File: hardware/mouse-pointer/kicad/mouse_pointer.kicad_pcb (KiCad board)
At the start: 2 copper layers, 23.5 x 31.5 mm, 24 parts, among them J1 Conn_PinHeader, J2 Conn_FPC, U1 PMW3610, U2 TLV74318PDBVR

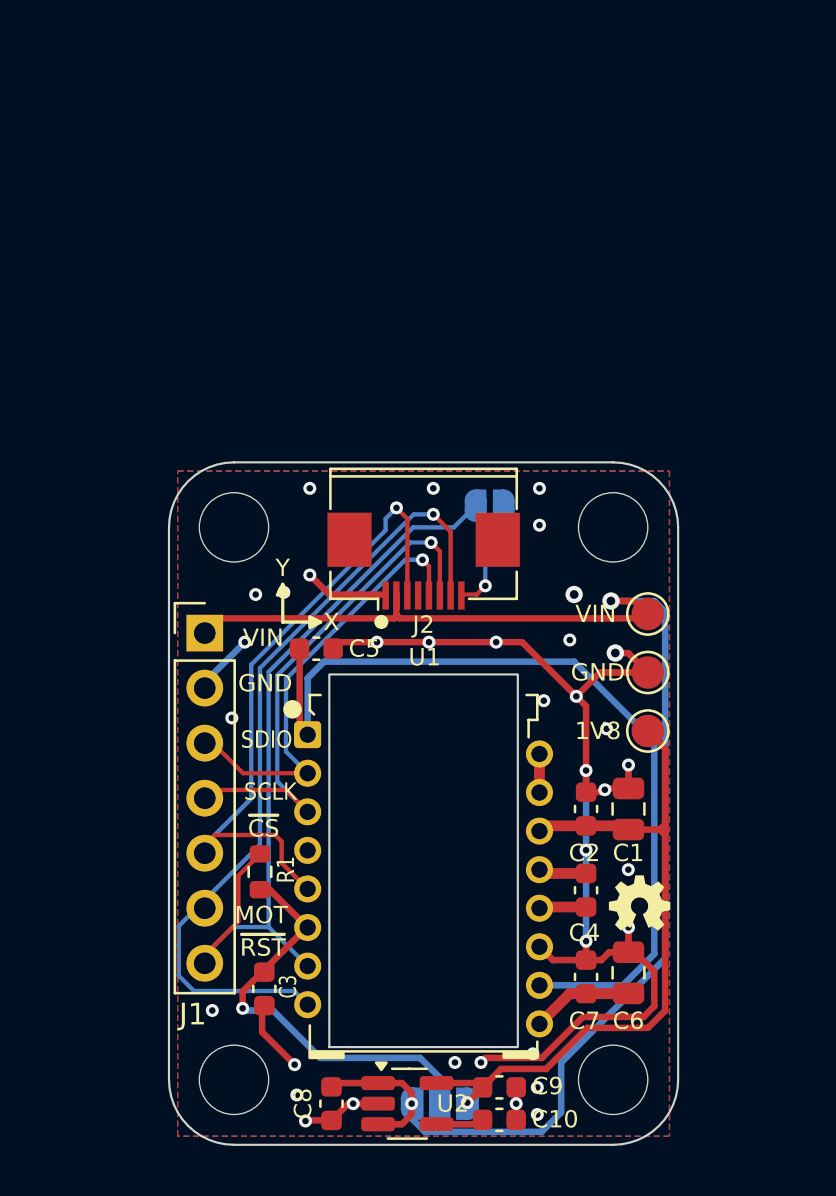
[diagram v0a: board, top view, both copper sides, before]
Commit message: feat: add RJ45 mouse pointer board interface
- Add the ClickTapToe 8P8C/RJ45 pinout to the PMW3610 mouse pointer board.
  - Add reset and VDDIO configuration links, optional nCS pull-up, and MOTION series resistor.
  - Extend the board layout for the RJ45 connector and added mounting holes.
  - Document revised mouse pointer cabling, twisted-pair grouping, and input hub wiring contract.
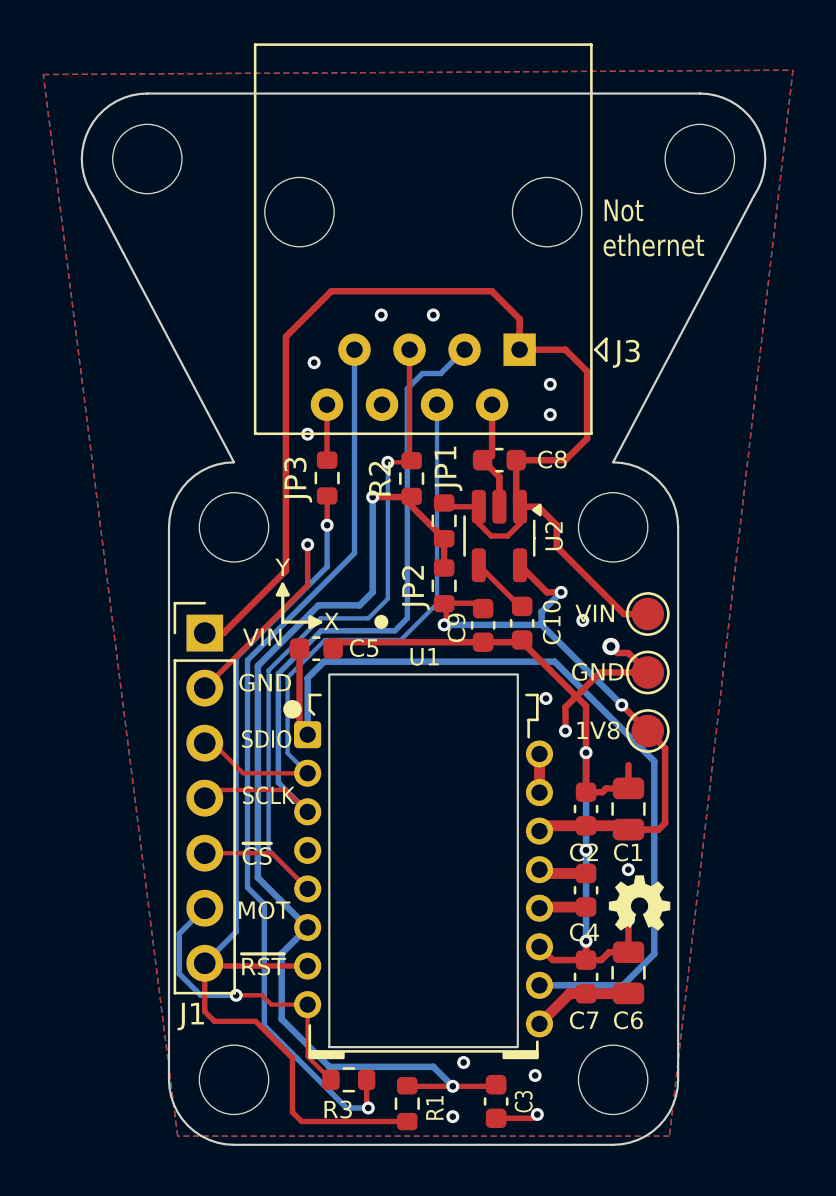
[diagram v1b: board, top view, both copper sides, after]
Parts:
- removed J2: Conn_FPC, mouse_pointer:FPC_8P_0.5mm_AFC01-S08FCA-00
- added H5: MountingHole, MountingHole:MountingHole_3.2mm_M3_ISO14580, B.Cu at (162.8, 70.2)
- added H6: MountingHole, MountingHole:MountingHole_3.2mm_M3_ISO14580, B.Cu at (137.2, 70.2)
- added J3: 8P8C, Connector_RJ:RJ45_Amphenol_54602-x08_Horizontal, F.Cu at (154.4, 79.0)
- added JP3: 0R, Resistor_SMD:R_0603_1608Metric, F.Cu at (145.6, 85.0)
- added R2: 100k, Resistor_SMD:R_0603_1608Metric, F.Cu at (149.4, 85.0)
- added R3: 100, Resistor_SMD:R_0603_1608Metric, F.Cu at (146.6, 112.8)
- JP1: value SolderJumper_3_Open -> 0R; footprint Jumper:SolderJumper-3_P1.3mm_Open_RoundedPad1.0x1.5mm_NumberLabels -> Resistor_SMD:R_0603_1608Metric; moved to F.Cu
- JP2: value FPC_RST -> 0R; footprint Jumper:SolderJumper-2_P1.3mm_Open_RoundedPad1.0x1.5mm -> Resistor_SMD:R_0603_1608Metric; moved to F.Cu
- moved C8 30.7 mm to (153.5, 84.2), turned to 180 degrees
- moved JP1 26.9 mm to (150.9, 87.0), turned to -90 degrees
- moved U2 26.5 mm to (153.5, 87.7), turned to -90 degrees
- moved C10 22.9 mm to (154.6, 91.7), turned to -90 degrees
- moved C9 21.3 mm to (152.8, 91.8), turned to -90 degrees
- moved R1 12.7 mm to (149.2, 113.8), turned to -90 degrees
- moved C3 11.9 mm to (153.3, 113.8)
- moved JP2 4.25 mm to (150.9, 90.0), turned to -90 degrees
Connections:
- JP2 pad 1: nRESET -> VDDIO
- JP2 pad 2: Net-(J2-Pin_8) -> +1V8
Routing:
- net MOT_RJ45: track 0.00 -> 41.3 mm, vias 0 -> 1
- net VDDIO: track 19.9 -> 48.3 mm, vias 1 -> 2
- net MOTION: track 37.4 -> 14.1 mm
- net VIN: track 66.4 -> 56.7 mm, vias 2 -> 0
- net SCLK: track 24.3 -> 33.1 mm, vias 1 -> 0
- net nRESET: track 36.3 -> 43.9 mm, vias 0 -> 1
- net SDIO: track 20.5 -> 27.8 mm, vias 1 -> 0
- net GND: track 66.4 -> 59.3 mm, vias 36 -> 20
- net nCS: track 30.0 -> 35.6 mm
- net Net-(J2-Pin_8): track 5.32 -> 0.00 mm, vias 1 -> 0
- net +1V8: track 33.4 -> 29.5 mm, vias 1 -> 3
- net nRST_RJ45: track 0.00 -> 2.56 mm
- net Net-(U2-NC): track 2.21 -> 2.79 mm
- net Net-(U1-+VCSEL): track 40.5 -> 40.0 mm
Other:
- board size 23.5 x 31.5 mm -> 31.5 x 48.5 mm
- board text added: "JP1: V_{DDIO}=VIN JP2: V_{DDIO}=1.8V JP1 + JP2: V_{DDIO}=VIN=VDD"
- board text added: "Not ethernet"
- board text removed: "JP1: [1-2 3]V_{DDIO}=VIN [1 2-3]V_{DDIO}=1.8V"

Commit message: fix: refine mouse pointer board layout
- Adjust board outline edges.
- Reposition components for improved decoupling
- Tune trace routing and via placement
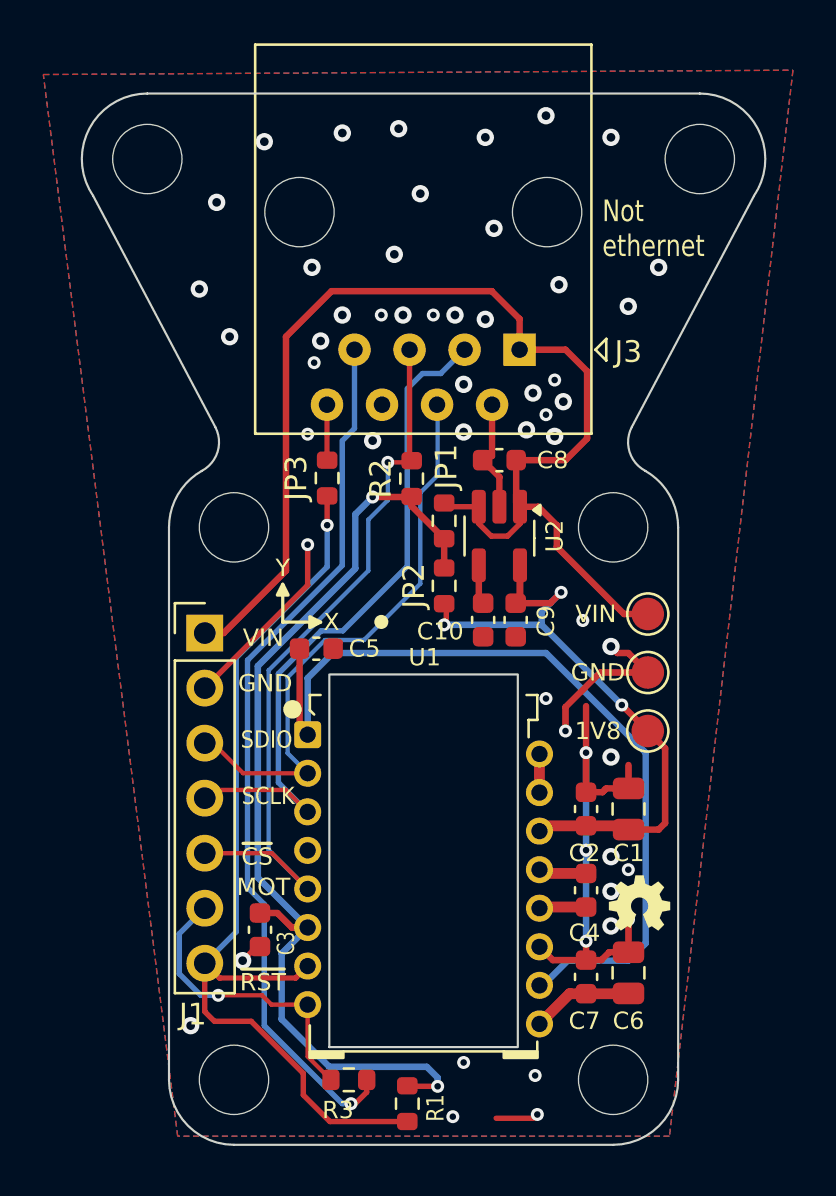
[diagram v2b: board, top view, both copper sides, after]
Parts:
- moved C3 13.5 mm to (142.4, 105.8)
- moved C10 1.81 mm to (152.8, 91.5)
- moved C9 1.52 mm to (154.2, 91.5)
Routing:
- net GND: track 59.3 -> 48.0 mm, vias 20 -> 54
- net VDDIO: track 48.3 -> 45.9 mm
- net SCLK: track 33.1 -> 31.7 mm
- net nCS: track 35.6 -> 34.4 mm
- net Net-(U2-NC): track 2.79 -> 1.55 mm
- net +1V8: track 29.5 -> 30.7 mm
- net SDIO: track 27.8 -> 26.8 mm
- net MOT_RJ45: track 41.3 -> 40.6 mm
- net Net-(U1-+VCSEL): track 40.0 -> 39.5 mm
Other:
- outline, holes or cut-outs redrawn

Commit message: feat: add ESD protection to mouse pointer and update board fields
- Add ESD protection, logo artwork, and final board manufacturing fields.
  - Include generated fabrication outputs for direct ordering.
  - Document hand-installed RJ45, optional tester header, and board configuration.
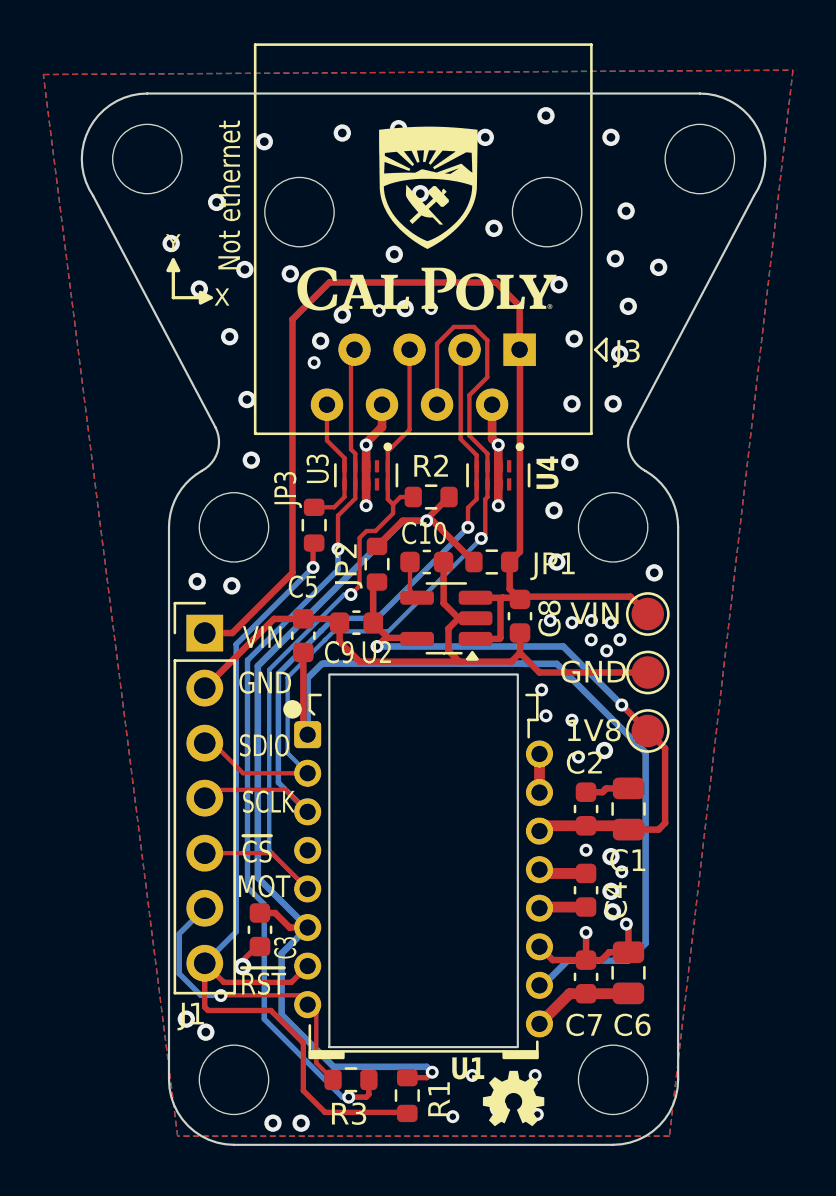
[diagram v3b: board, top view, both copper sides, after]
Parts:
- added U3: TPD4E05U06DQAR, mouse_pointer:IC_TPD4E05U06DQAR, F.Cu at (147.3, 84.8)
- added U4: TPD4E05U06DQAR, mouse_pointer:IC_TPD4E05U06DQAR, F.Cu at (153.4, 84.8)
- H3, H5, H6: moved to F.Cu
- moved C9 7.35 mm to (146.9, 91.7), turned to 180 degrees
- moved C8 7.26 mm to (154.4, 91.3), turned to -90 degrees
- moved U2 4.52 mm to (151.1, 91.5), turned to 180 degrees
- moved C10 3.73 mm to (150.2, 88.8), turned to 0 degrees
- moved JP2 3.26 mm to (147.8, 89.0)
- moved JP1 2.91 mm to (153.2, 88.8), turned to 180 degrees
- moved JP3 2.26 mm to (144.9, 87.2)
- moved R2 1.24 mm to (150.3, 85.8), turned to 180 degrees
- moved C5 0.85 mm to (144.4, 92.2), turned to 90 degrees
- moved R1 0.38 mm to (149.2, 113.5)
- moved R3 0.10 mm to (146.7, 112.8)
- turned H3 to 0 degrees
- turned H5 to 0 degrees
- turned H6 to 0 degrees
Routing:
- net SDIO: track 26.8 -> 37.6 mm, vias 0 -> 1
- net nRST_RJ45: track 2.56 -> 6.19 mm
- net GND: track 48.0 -> 51.2 mm, vias 54 -> 71
- net nRESET: track 43.4 -> 41.3 mm
- net VIN: track 56.7 -> 54.6 mm
- net nCS: track 34.4 -> 35.5 mm
- net VDDIO: track 45.9 -> 47.0 mm
- net +1V8: track 30.7 -> 29.8 mm, vias 3 -> 2
- net SCLK: track 31.7 -> 32.4 mm, vias 0 -> 1
- net MOT_RJ45: track 40.6 -> 40.5 mm, vias 1 -> 2

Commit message: feat: updated board for JLC constraints, add 3D models, add silkscreen logos, correct production outputs
- Add Cal Poly and EMPOWER silkscreen artwork and generated KiCad footprints.
  - Add PMW3610 and RJ45 model assets for board review.
  - Update JLC board constraints and clean up resulting DRC issues.
  - Update ESD placement rotation fields for JLC assembly output.
  - Exclude optional headers, RJ45s, DNP parts, test points, and holes from assembly files.
  - Regenerate mouse pointer production BOM, CPL, netlist, and fabrication archive.
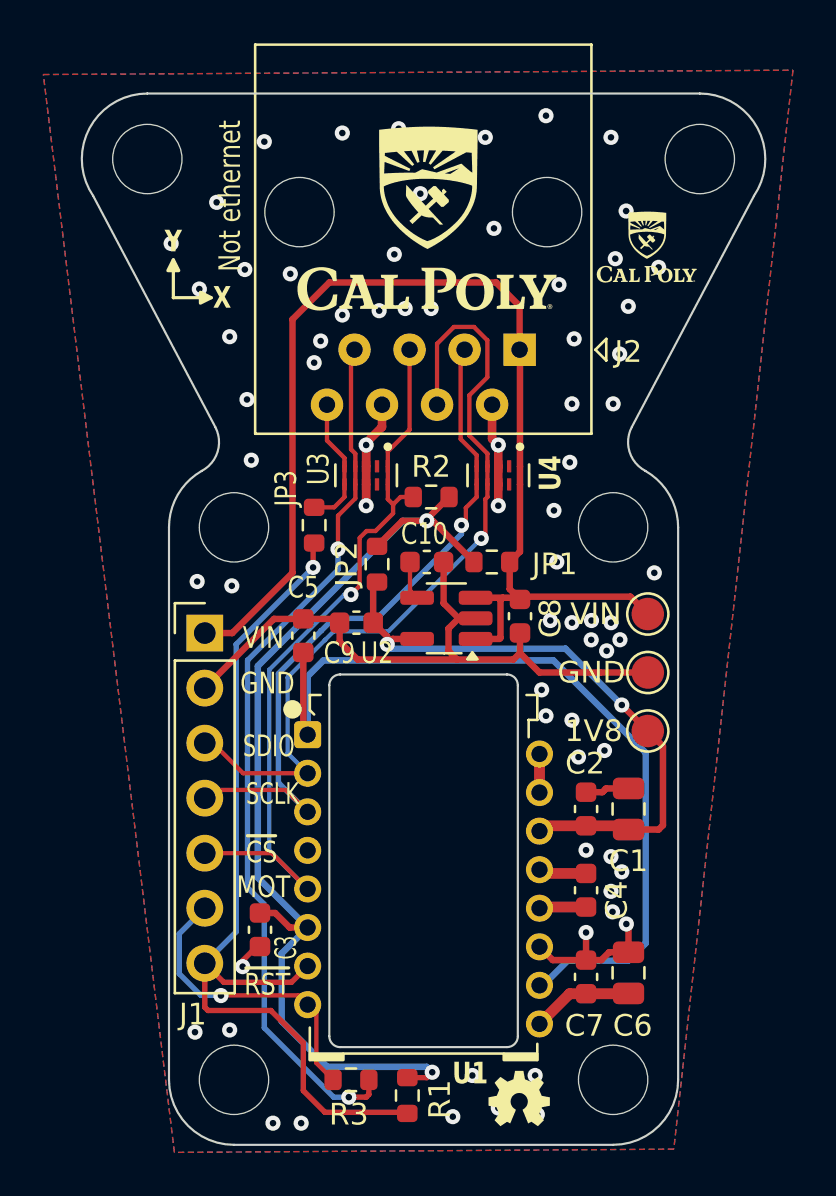
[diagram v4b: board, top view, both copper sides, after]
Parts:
- added G***: EMPOWER_Hand_Line_Silkscreen_7mm_MildSmooth, mouse_pointer:EMPOWER_Hand_Line_Silkscreen_7mm_MildSmooth, B.Cu at (159.9, 74.8)
- J2: renamed from J3; value 8P8C -> 54602-908LF; footprint Connector_RJ:RJ45_Amphenol_54602-x08_Horizontal -> mouse_pointer:RJ45_Amphenol_54602-x08_Horizontal
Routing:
- net +1V8: track 29.8 -> 29.0 mm
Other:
- board text added: "${COMPANY} ClickTapToe ${TITLE} Rev ${REVISION} June 2026"
- board text removed: "${COMPANY} ${TITLE} Rev ${REVISION}"
